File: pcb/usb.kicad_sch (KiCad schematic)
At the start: 9 parts, among them J2 USB_C_Receptacle_USB2.0, Q1 MMBT3906

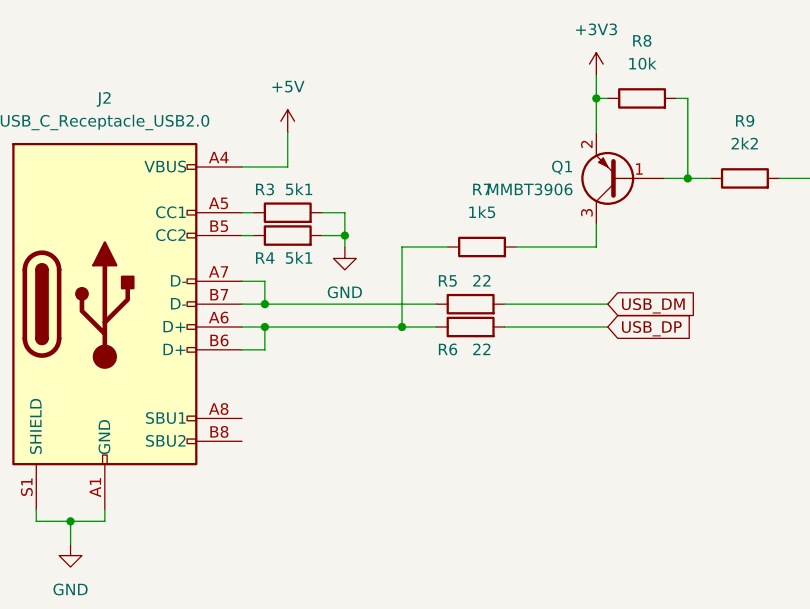
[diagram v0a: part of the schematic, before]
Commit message: cleaned up symbols in schematics a bit
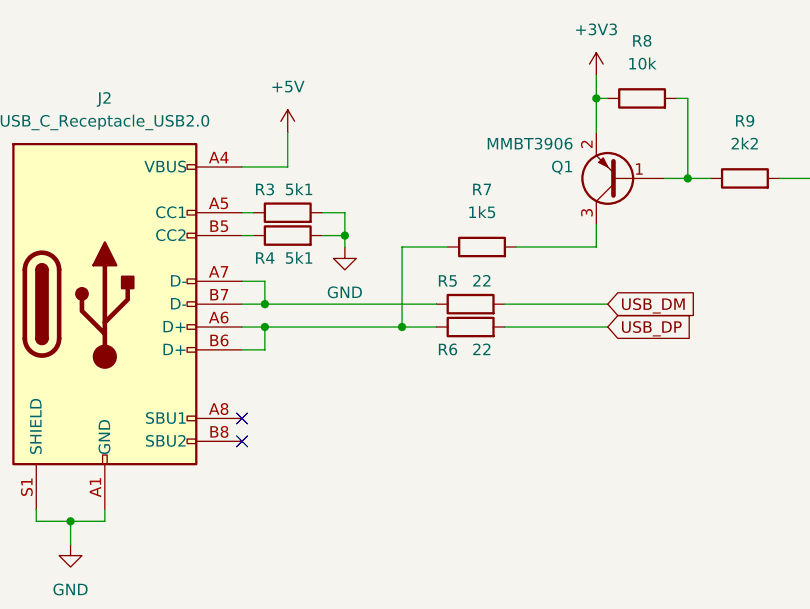
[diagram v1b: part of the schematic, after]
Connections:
- no-connect marks 0 -> 2
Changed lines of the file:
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@@
   (junction (at 100.33 97.79) (diameter 0) (color 0 0 0 0)
   )
+  (no_connect (at 82.55 107.95))
+  (no_connect (at 82.55 110.49))
   (wire (pts (xy 91.44 85.09) (xy 93.98 85.09))
     (stroke (width 0) (type default) (color 0 0 0 0))
@@
   )
   (symbol (lib_id "Transistor_BJT:MMBT3906") (at 124.46 81.28 180) (unit 1)
-    (in_bom yes) (on_board yes) (fields_autoplaced)
+    (in_bom yes) (on_board yes)
     (property "Reference" "Q1" (id 0) (at 119.38 80.0099 0)
       (effects (font (size 1.27 1.27)) (justify left))
     )
-    (property "Value" "MMBT3906" (id 1) (at 119.38 82.5499 0)
+    (property "Value" "MMBT3906" (id 1) (at 119.38 77.47 0)
       (effects (font (size 1.27 1.27)) (justify left))
     )

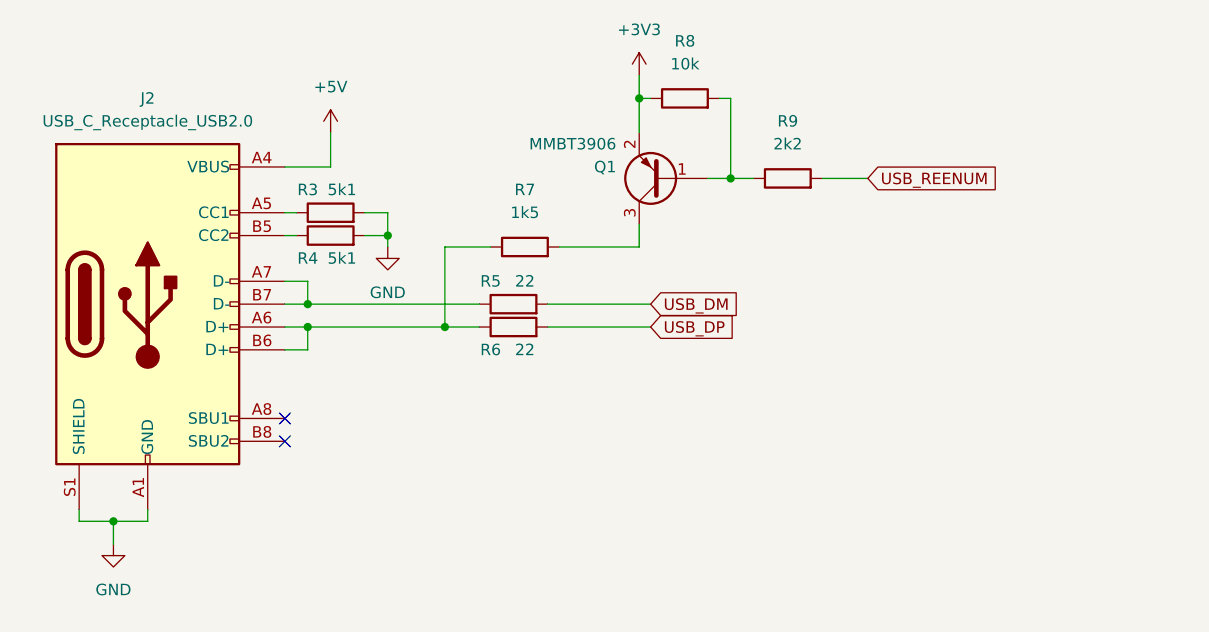
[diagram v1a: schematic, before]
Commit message: - split schematic to lists - changed global ports to local - assigned footprints to majority of schematic parts
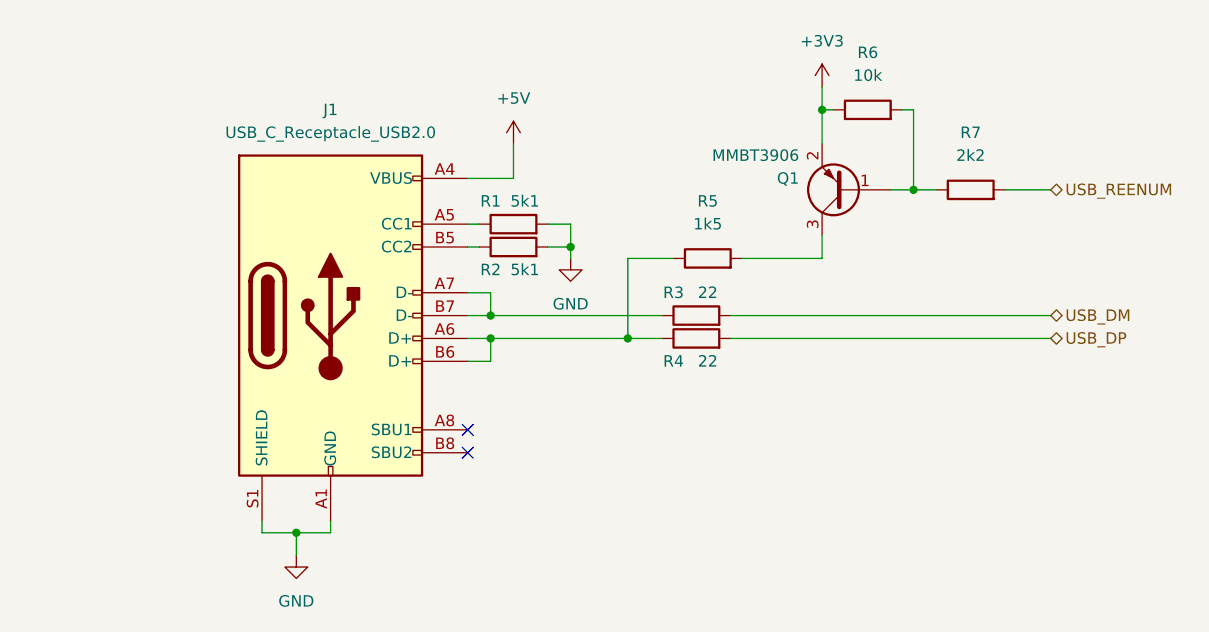
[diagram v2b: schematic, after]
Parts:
- J1: renamed from J2; footprint (none) -> Connector_USB:USB_C_Receptacle_HRO_TYPE-C-31-M-12
- R1: renamed from R3; footprint (none) -> Resistor_SMD:R_0603_1608Metric
- R2: renamed from R4; footprint (none) -> Resistor_SMD:R_0603_1608Metric
- R3: renamed from R5; footprint (none) -> Resistor_SMD:R_0603_1608Metric
- R4: renamed from R6; footprint (none) -> Resistor_SMD:R_0603_1608Metric
- R5: renamed from R7; footprint (none) -> Resistor_SMD:R_0603_1608Metric
- R6: renamed from R8; footprint (none) -> Resistor_SMD:R_0603_1608Metric
- R7: renamed from R9; footprint (none) -> Resistor_SMD:R_0603_1608Metric
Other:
- moved on the sheet: J1, Q1, R1, R2, R3, R4, R5, R6, R7

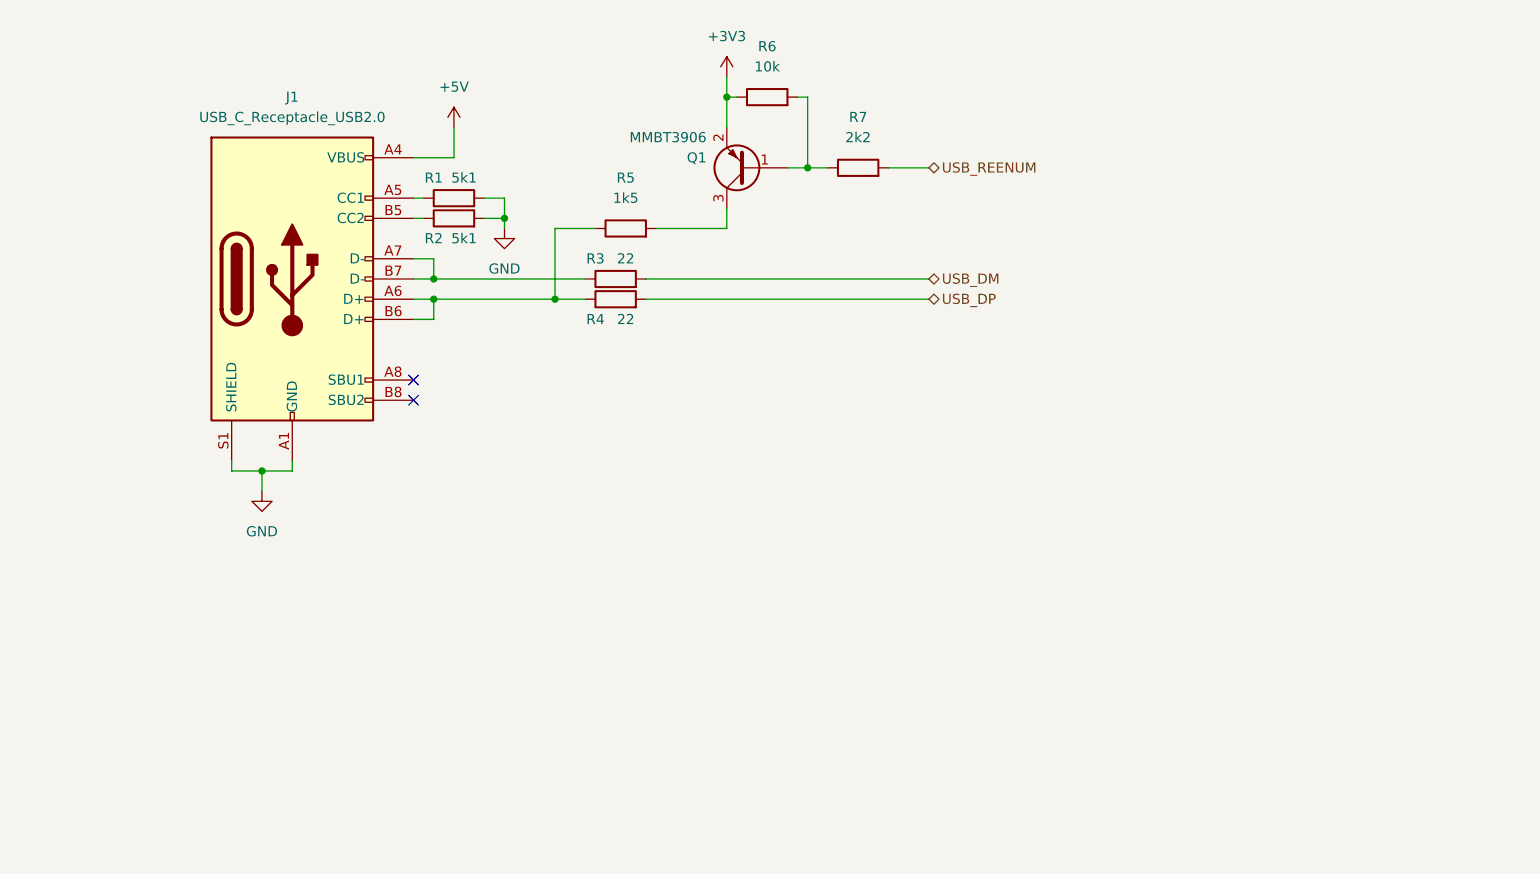
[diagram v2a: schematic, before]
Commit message: - added debouncing to buttons - assigned some footprints - added expansion and inspection pin headers
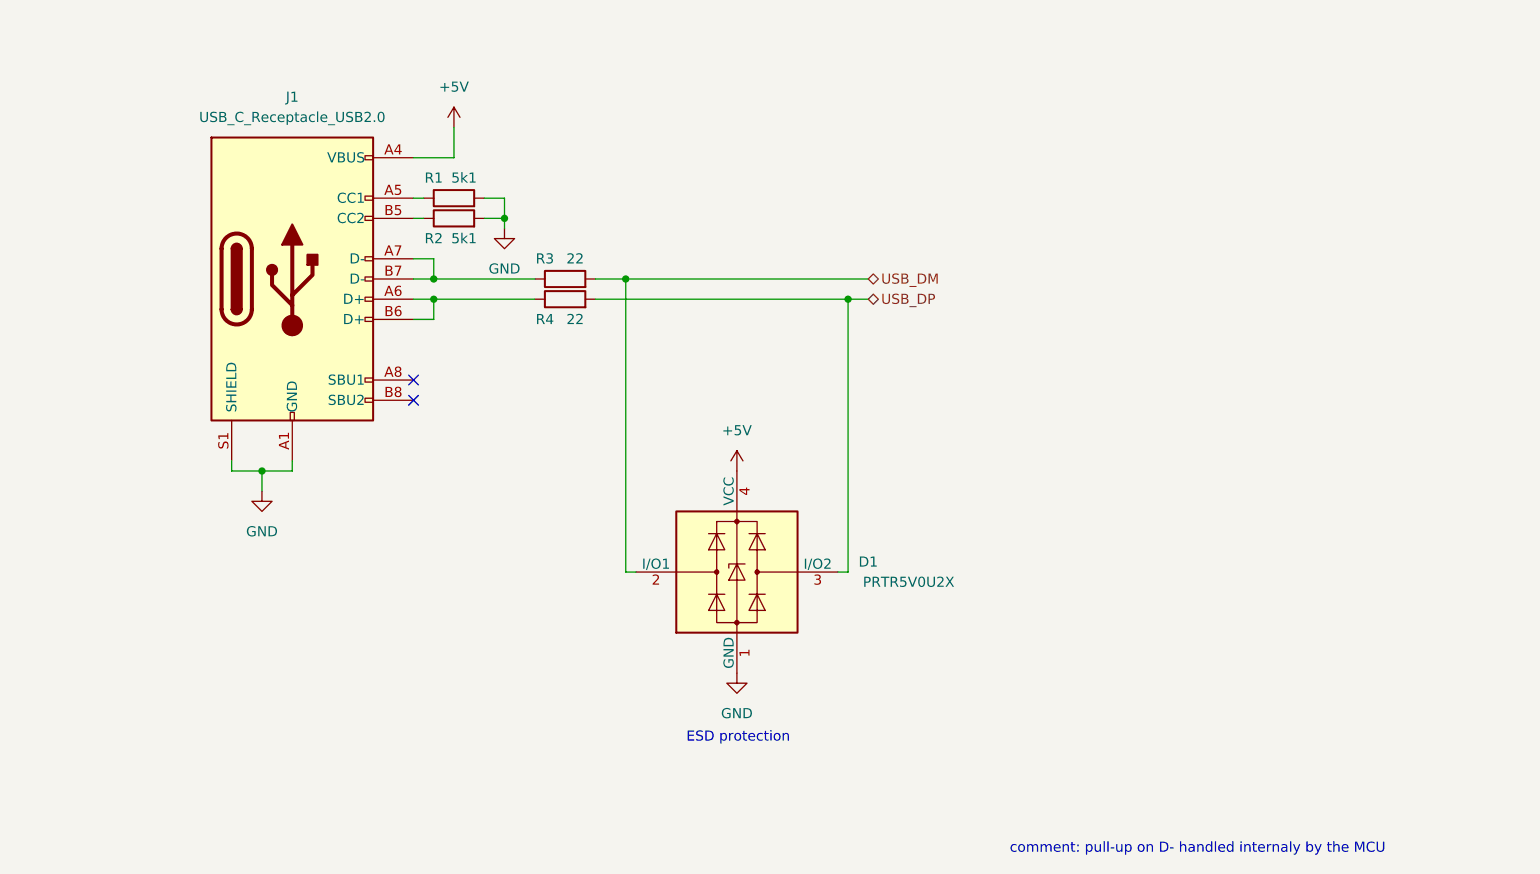
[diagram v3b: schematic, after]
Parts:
- removed Q1: MMBT3906, Package_TO_SOT_SMD:SOT-23, symbol Transistor_BJT:MMBT3906
- removed R5: 1k5, Resistor_SMD:R_0603_1608Metric, symbol Device:R
- removed R6: 10k, Resistor_SMD:R_0603_1608Metric, symbol Device:R
- removed R7: 2k2, Resistor_SMD:R_0603_1608Metric, symbol Device:R
- added D1: PRTR5V0U2X, Package_TO_SOT_SMD:SOT-143, symbol Power_Protection:PRTR5V0U2X
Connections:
- net +5V: now also D1.4 (VCC)
- net GND: now also D1.1 (GND)
- net USB_DM: now also D1.2 (I/O1)
- net USB_DP: now also D1.3 (I/O2)
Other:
- note added: "ESD protection"
- note added: "comment: pull-up on D- handled internaly by the MCU"
- moved on the sheet: R3, R4

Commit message: added LCSC part numbers and assigned footprints
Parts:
- D1: LCSC (none) -> C2827688
- J1: footprint Connector_USB:USB_C_Receptacle_HRO_TYPE-C-31-M-12 -> Connector_USB:USB_C_Receptacle_XKB_U262-16XN-4BVC11; LCSC (none) -> C319148
- R1, R2: LCSC (none) -> C23186
- R3, R4: LCSC (none) -> C107701
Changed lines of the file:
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@@
+      (effects (font (size 1.27 1.27)) hide)
+    )
+    (property "LCSC" "C107701" (id 4) (at 121.92 99.06 0)
       (effects (font (size 1.27 1.27)) hide)
     )
@@
     )
     (property "Datasheet" "~" (id 3) (at 107.95 88.9 0)
+      (effects (font (size 1.27 1.27)) hide)
+    )
+    (property "LCSC" "C23186" (id 4) (at 107.95 88.9 0)
       (effects (font (size 1.27 1.27)) hide)
     )
@@
       (effects (font (size 1.27 1.27)) hide)
     )
+    (property "LCSC" "C2827688" (id 4) (at 143.51 133.35 0)
+      (effects (font (size 1.27 1.27)) hide)
+    )
     (pin "1")
     (pin "2")
@@
     )
     (property "Datasheet" "~" (id 3) (at 121.92 96.52 0)
+      (effects (font (size 1.27 1.27)) hide)
+    )
+    (property "LCSC" "C107701" (id 4) (at 121.92 96.52 0)
       (effects (font (size 1.27 1.27)) hide)
     )
@@
       (effects (font (size 1.27 1.27)) hide)
     )
+    (property "LCSC" "C23186" (id 4) (at 107.95 86.36 0)
+      (effects (font (size 1.27 1.27)) hide)
+    )
     (pin "1")
     (pin "2")
@@
     (property "Reference" "J1" (id 0) (at 87.63 73.66 0))
     (property "Value" "USB_C_Receptacle_USB2.0" (id 1) (at 87.63 76.2 0))
-    (property "Footprint" "Connector_USB:USB_C_Receptacle_HRO_TYPE-C-31-M-12" (id 2) (at 91.44 96.52 0)
+    (property "Footprint" "Connector_USB:USB_C_Receptacle_XKB_U262-16XN-4BVC11" (id 2) (at 91.44 96.52 0)
       (effects (font (size 1.27 1.27)) hide)
     )
@@
       (effects (font (size 1.27 1.27)) hide)
     )
+    (property "LCSC" "C319148" (id 4) (at 87.63 96.52 0)
+      (effects (font (size 1.27 1.27)) hide)
+    )

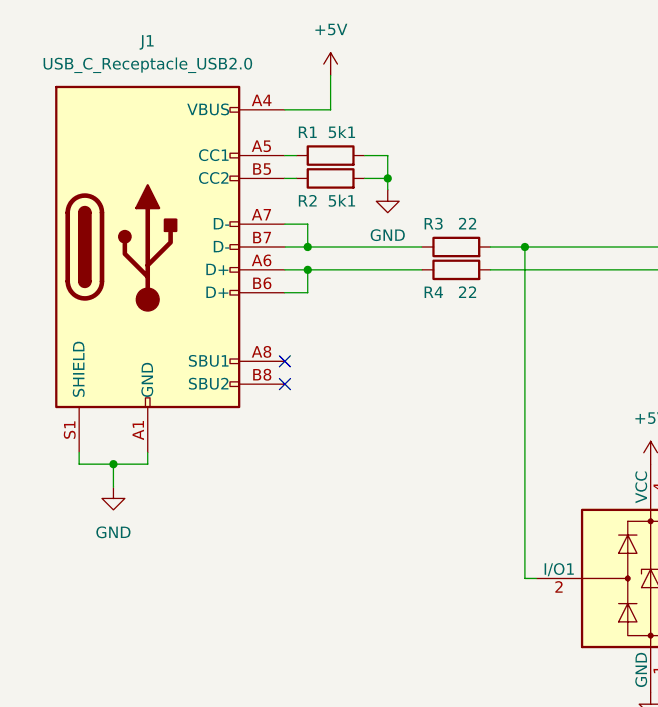
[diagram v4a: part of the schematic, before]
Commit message: added PWR_FLAGs to pass ERC checks
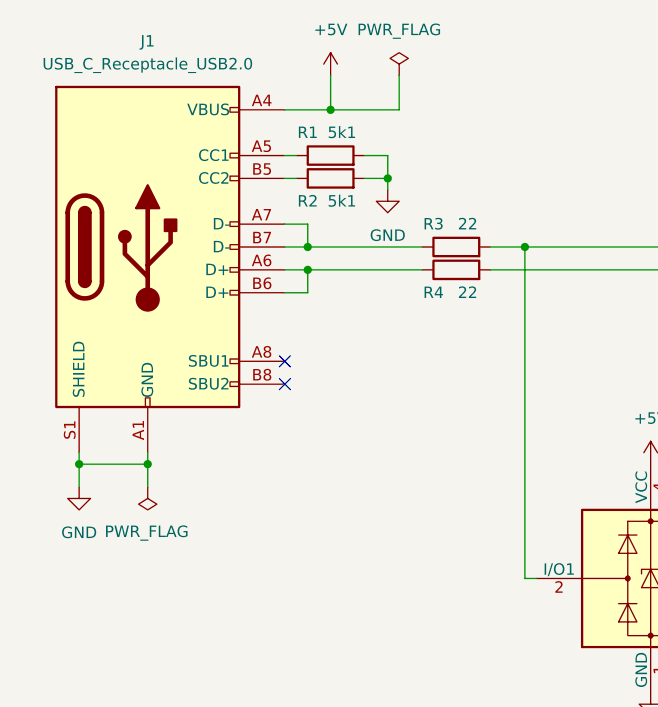
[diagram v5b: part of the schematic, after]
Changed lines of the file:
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@@
 (kicad_sch (version 20211123) (generator eeschema)
   (paper "A4")
-  (junction (at 83.82 120.65) (diameter 0) (color 0 0 0 0)
+  (junction (at 80.01 120.65) (diameter 0) (color 0 0 0 0)
   )
   (junction (at 114.3 88.9) (diameter 0) (color 0 0 0 0)
@@
   (junction (at 129.54 96.52) (diameter 0) (color 0 0 0 0)
   )
+  (junction (at 107.95 81.28) (diameter 0) (color 0 0 0 0)
+  )
   (junction (at 105.41 96.52) (diameter 0) (color 0 0 0 0)
   )
   (junction (at 105.41 99.06) (diameter 0) (color 0 0 0 0)
+  )
+  (junction (at 87.63 120.65) (diameter 0) (color 0 0 0 0)
   )
   (no_connect (at 102.87 109.22))
@@
     (stroke (width 0) (type default) (color 0 0 0 0))
   )
+  (wire (pts (xy 115.57 77.47) (xy 115.57 81.28))
+    (stroke (width 0) (type default) (color 0 0 0 0))
+  )
   (wire (pts (xy 87.63 120.65) (xy 87.63 119.38))
     (stroke (width 0) (type default) (color 0 0 0 0))
@@
     (stroke (width 0) (type default) (color 0 0 0 0))
   )
-  (wire (pts (xy 83.82 120.65) (xy 87.63 120.65))
+  (wire (pts (xy 87.63 120.65) (xy 87.63 123.19))
     (stroke (width 0) (type default) (color 0 0 0 0))
   )
@@
     (stroke (width 0) (type default) (color 0 0 0 0))
   )
-  (wire (pts (xy 80.01 120.65) (xy 83.82 120.65))
+  (wire (pts (xy 80.01 120.65) (xy 87.63 120.65))
     (stroke (width 0) (type default) (color 0 0 0 0))
   )
@@
     (stroke (width 0) (type default) (color 0 0 0 0))
   )
-  (wire (pts (xy 83.82 120.65) (xy 83.82 123.19))
-    (stroke (width 0) (type default) (color 0 0 0 0))
-  )
   (wire (pts (xy 157.48 99.06) (xy 160.02 99.06))
     (stroke (width 0) (type default) (color 0 0 0 0))
@@
     (stroke (width 0) (type default) (color 0 0 0 0))
   )
+  (wire (pts (xy 115.57 81.28) (xy 107.95 81.28))
+    (stroke (width 0) (type default) (color 0 0 0 0))
+  )
   (wire (pts (xy 114.3 88.9) (xy 114.3 90.17))
     (stroke (width 0) (type default) (color 0 0 0 0))
@@
   )
   (wire (pts (xy 107.95 81.28) (xy 107.95 77.47))
+    (stroke (width 0) (type default) (color 0 0 0 0))
+  )
+  (wire (pts (xy 80.01 120.65) (xy 80.01 123.19))
     (stroke (width 0) (type default) (color 0 0 0 0))
   )
@@
     (pin "1")
   )
-  (symbol (lib_id "power:GND") (at 83.82 123.19 0) (unit 1)
+  (symbol (lib_id "power:GND") (at 80.01 123.19 0) (unit 1)
     (in_bom yes) (on_board yes) (fields_autoplaced)
-    (property "Reference" "#PWR01" (id 0) (at 83.82 129.54 0)
-      (effects (font (size 1.27 1.27)) hide)
-    )
-    (property "Value" "GND" (id 1) (at 83.82 128.27 0))
-    (property "Footprint" "" (id 2) (at 83.82 123.19 0)
-      (effects (font (size 1.27 1.27)) hide)
-    )
-    (property "Datasheet" "" (id 3) (at 83.82 123.19 0)
+    (property "Reference" "#PWR01" (id 0) (at 80.01 129.54 0)
+      (effects (font (size 1.27 1.27)) hide)
+    )
+    (property "Value" "GND" (id 1) (at 80.01 128.27 0))
+    (property "Footprint" "" (id 2) (at 80.01 123.19 0)
+      (effects (font (size 1.27 1.27)) hide)
+    )
+    (property "Datasheet" "" (id 3) (at 80.01 123.19 0)
       (effects (font (size 1.27 1.27)) hide)
     )
@@
     (pin "1")
     (pin "2")
+  )
+  (symbol (lib_id "power:PWR_FLAG") (at 87.63 123.19 180) (unit 1)
+    (in_bom yes) (on_board yes)
+    (property "Reference" "#FLG0102" (id 0) (at 87.63 125.095 0)
+      (effects (font (size 1.27 1.27)) hide)
+    )
+    (property "Value" "PWR_FLAG" (id 1) (at 82.8287 128.156 0)
+      (effects (font (size 1.27 1.27)) (justify right))
+    )
+    (property "Footprint" "" (id 2) (at 87.63 123.19 0)
+      (effects (font (size 1.27 1.27)) hide)
+    )
+    (property "Datasheet" "~" (id 3) (at 87.63 123.19 0)
+      (effects (font (size 1.27 1.27)) hide)
+    )
+    (pin "1")
   )
   (symbol (lib_id "power:GND") (at 114.3 90.17 0) (unit 1)
@@
     (pin "S1")
   )
+  (symbol (lib_id "power:PWR_FLAG") (at 115.57 77.47 0) (unit 1)
+    (in_bom yes) (on_board yes) (fields_autoplaced)
+    (property "Reference" "#FLG0101" (id 0) (at 115.57 75.565 0)
+      (effects (font (size 1.27 1.27)) hide)
+    )
+    (property "Value" "PWR_FLAG" (id 1) (at 115.57 72.39 0))
+    (property "Footprint" "" (id 2) (at 115.57 77.47 0)
+      (effects (font (size 1.27 1.27)) hide)
+    )
+    (property "Datasheet" "~" (id 3) (at 115.57 77.47 0)
+      (effects (font (size 1.27 1.27)) hide)
+    )
+    (pin "1")
+  )
   (symbol (lib_id "power:+5V") (at 107.95 77.47 0) (unit 1)
